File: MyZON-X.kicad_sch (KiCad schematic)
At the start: 29 parts, among them J1 Connector ZX81, J2 Audio, J3 SJ1-3523N, SW1 SW_DIP_x03, U1 AY-3-8910, U2.1 74HCT74, U3.1 74HCT08, U4.1 74HCT11, U5.1 74HCT02

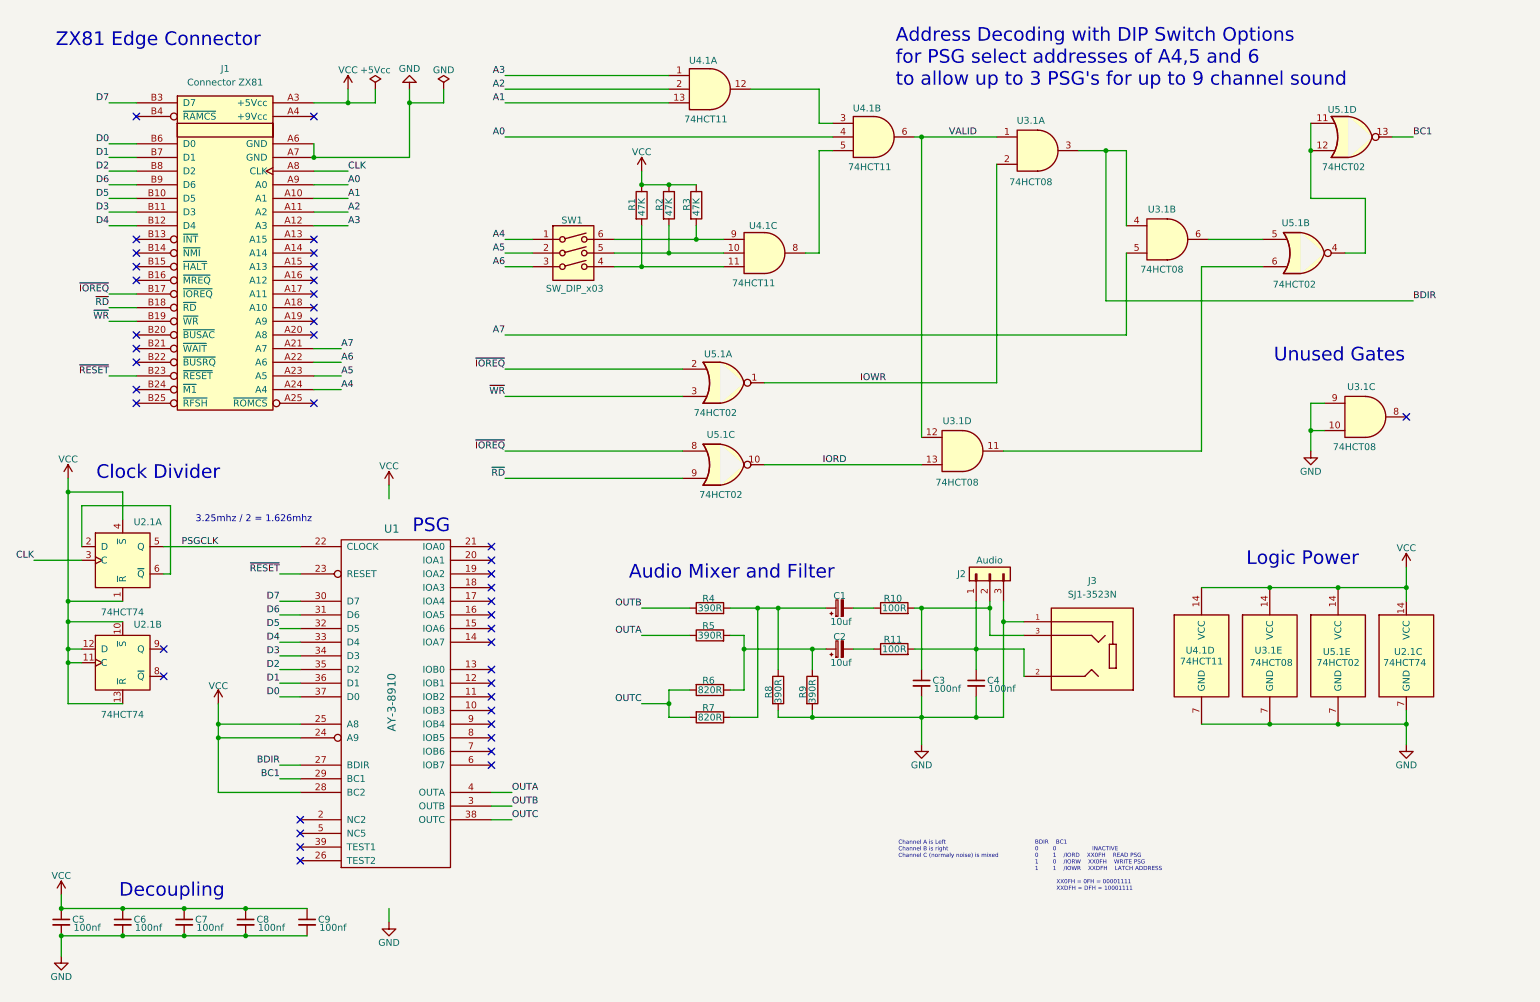
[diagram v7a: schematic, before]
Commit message: Routed PCB first pass Updated footprint for Audio Line Out Jack Added 3D model for Audio Line Out Jack Updated Schematic PDF Updated 3D Image
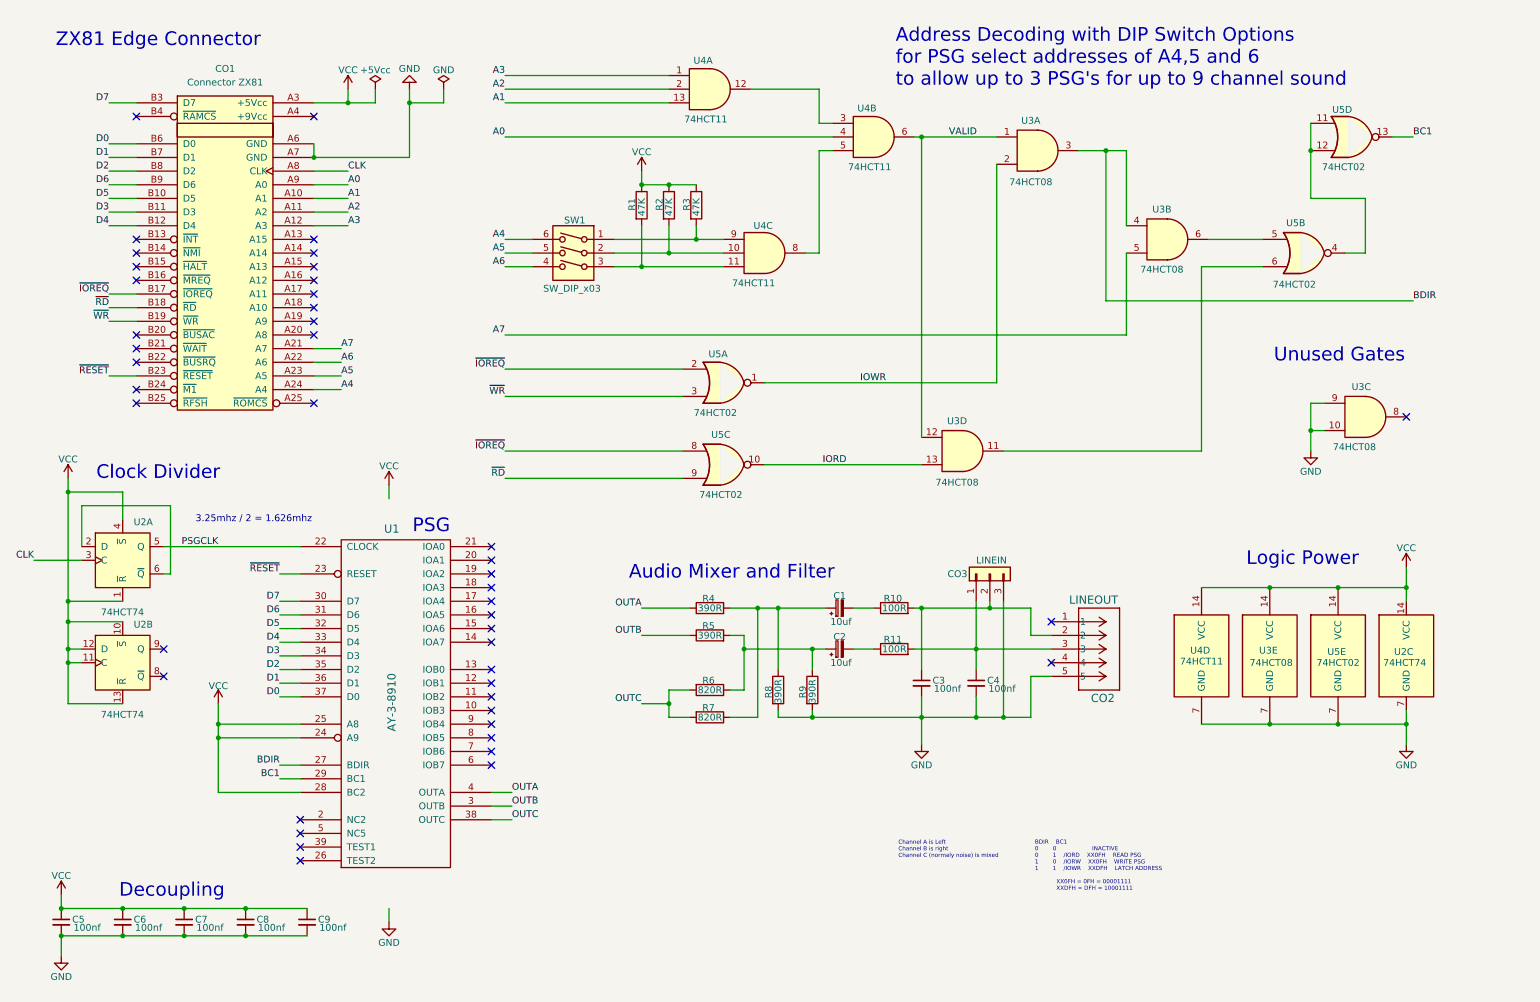
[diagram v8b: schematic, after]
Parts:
- removed J3: SJ1-3523N, AudioJack:CUI_SJ1-3523N, symbol AudioJack:SJ1-3523N
- added CO2: LINEOUT, AudioJack:CONN5_SPC21348_MTC, symbol AudioJack:SPC21348
- CO3: renamed from J2; value Audio -> LINEIN
- renumbered J1 to CO1, U2.1 to U2, U3.1 to U3, U4.1 to U4, U5.1 to U5
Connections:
- net A4: now also SW1.6; no longer SW1.1
- net A5: now also SW1.5; no longer SW1.2
- net A6: now also SW1.4; no longer SW1.3
- net GND: now also CO2.5
- net OUTA: now also R4.1; no longer R5.1
- net OUTB: now also R5.1; no longer R4.1
- net at C4.1, CO3.1 (Pin_1), R11.2: now also CO2.3
- net at R2.2, U4.10: now also SW1.2; no longer SW1.5
- net at R1.2, U4.11: now also SW1.3; no longer SW1.4
- net at R3.2, U4.9: now also SW1.1; no longer SW1.6
- net at C3.1, CO3.2 (Pin_2), R10.2: now also CO2.2
- no-connect marks 43 -> 45
